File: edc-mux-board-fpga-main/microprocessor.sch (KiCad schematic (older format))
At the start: 27 parts, among them J28 PRG/SWD, J29 USB PRG, Q4 CSD22206W, Q5 CSD22206W, SW3 Reset (Microprocessor), U64 TPD3S014, U65 SAMD21JXXAM, U66 MCP1812, U67 LTC4412

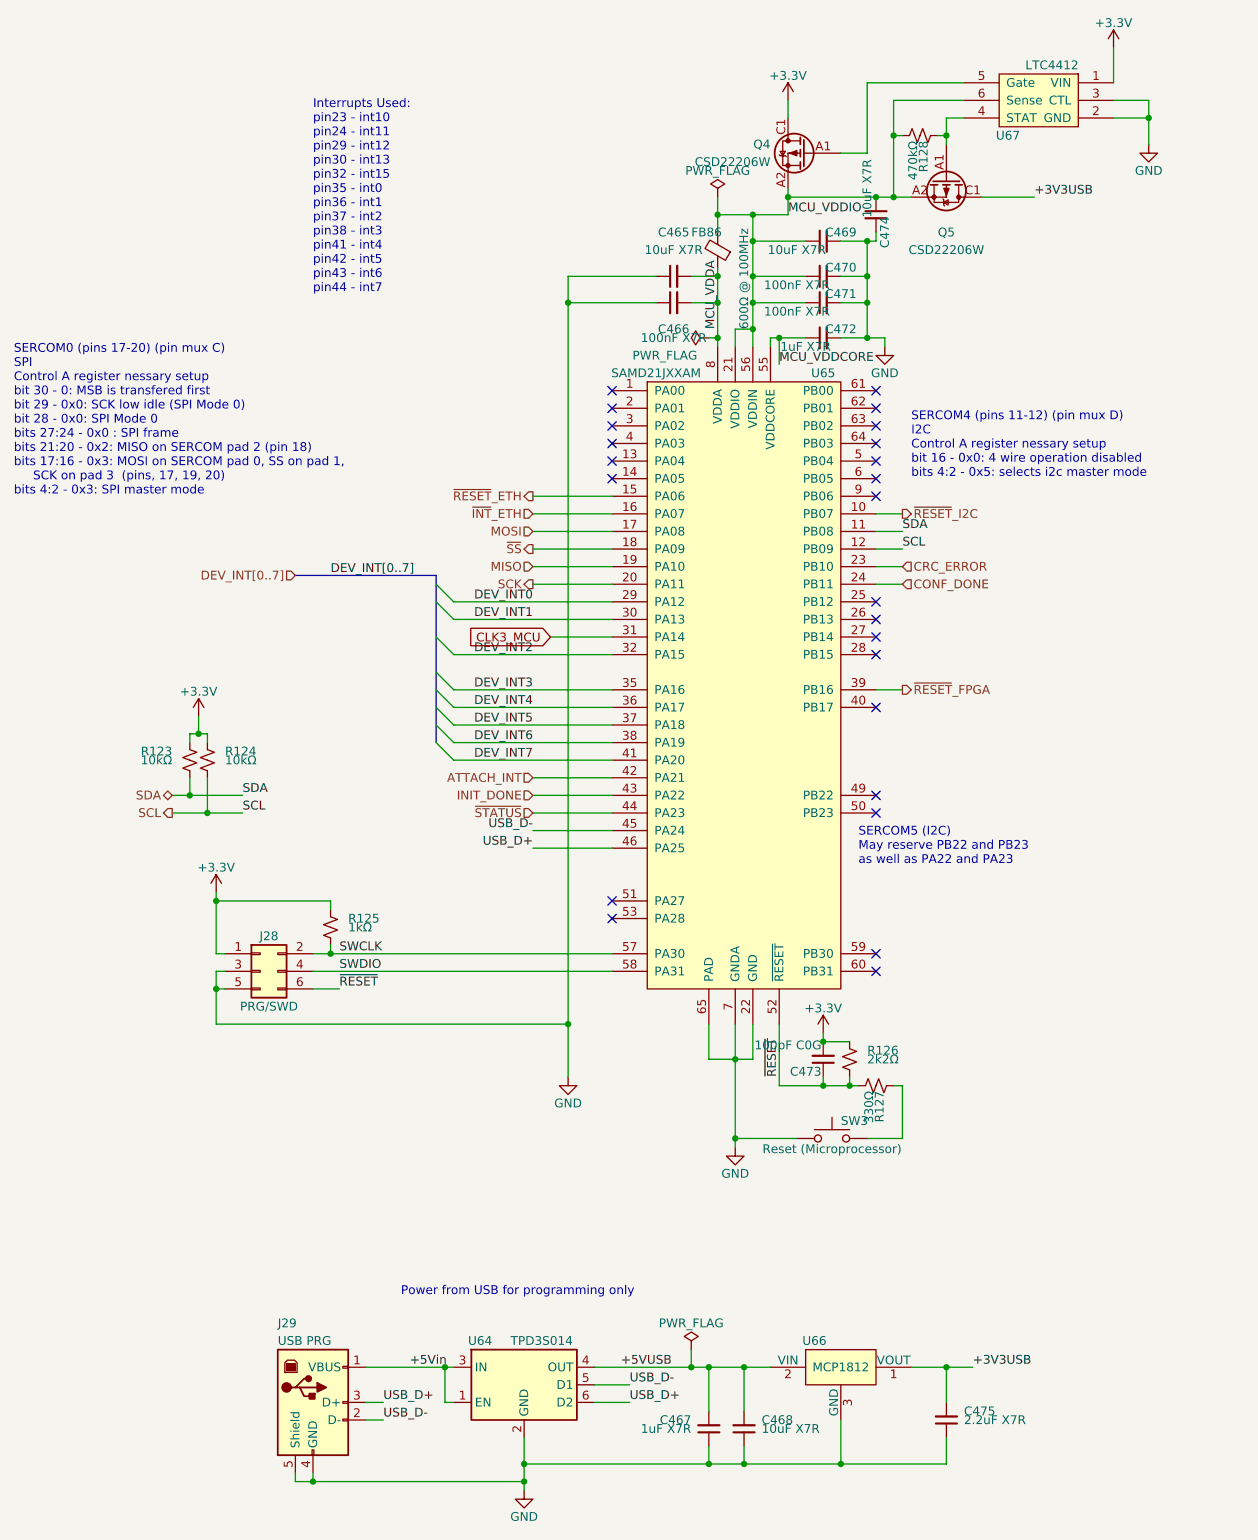
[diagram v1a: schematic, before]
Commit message: Reannotate main schematic and pcb after expansion transition
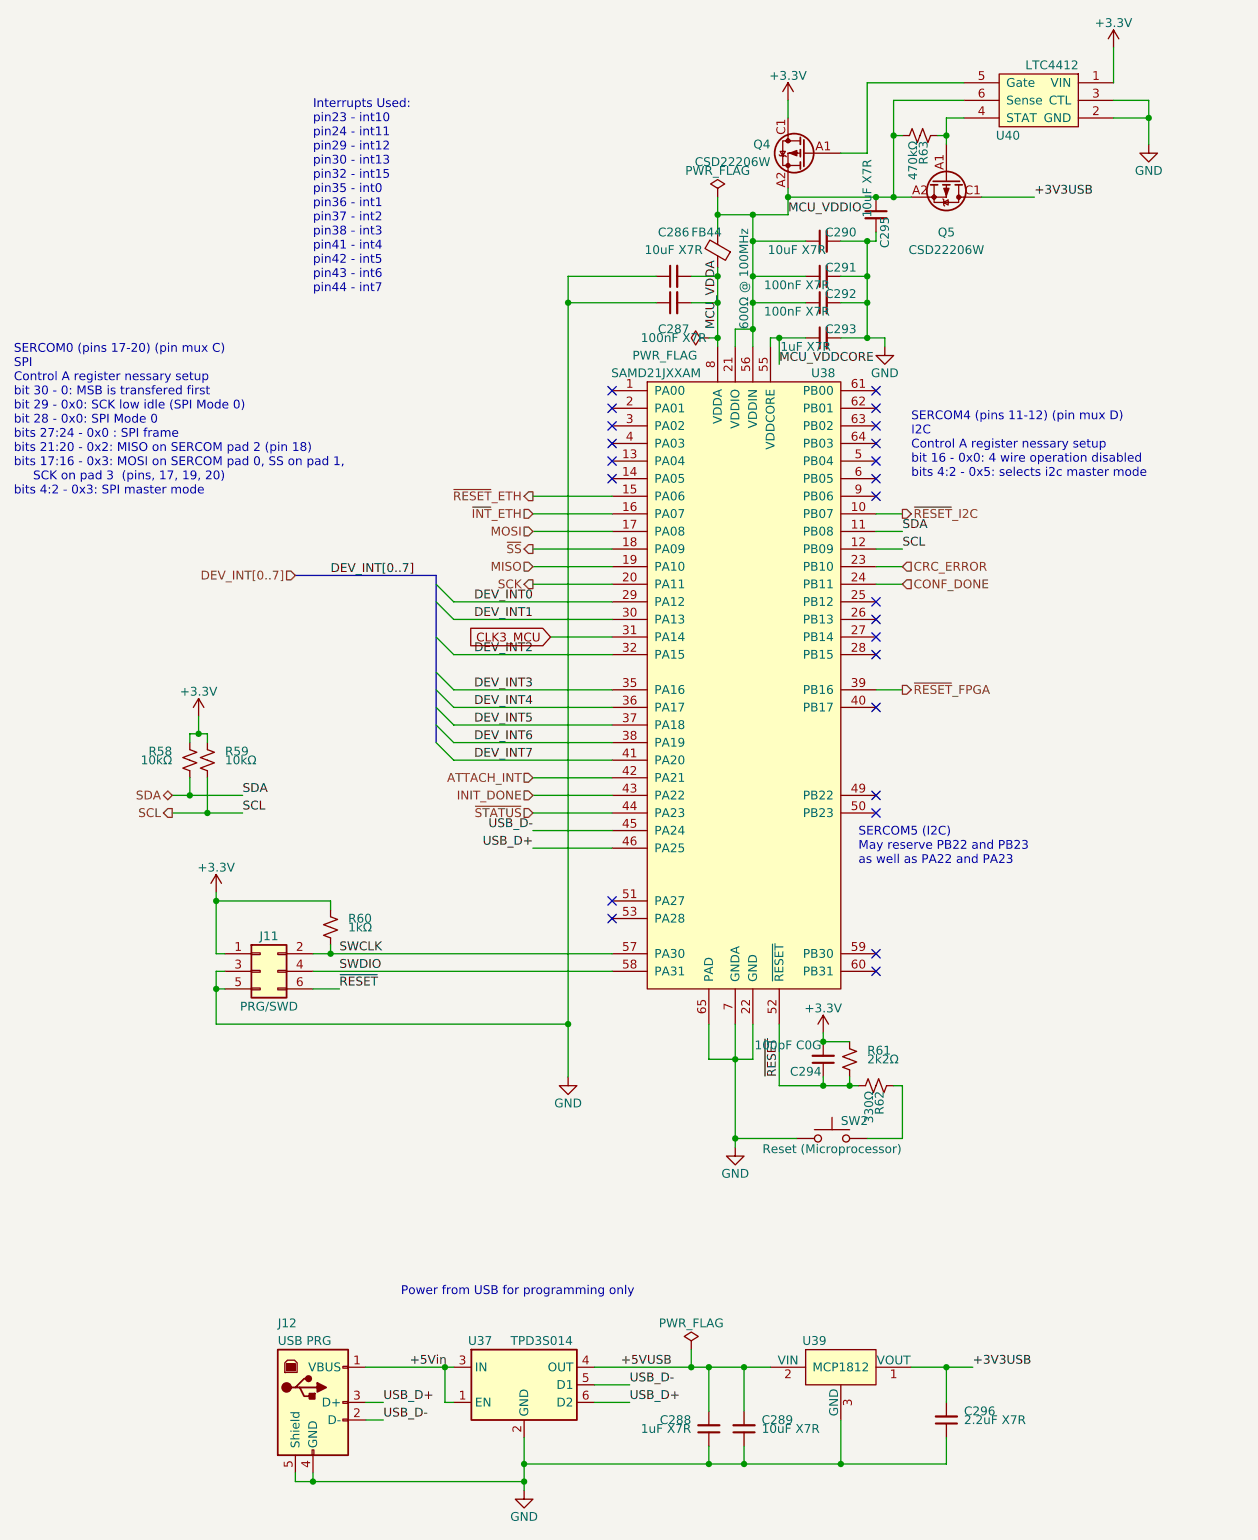
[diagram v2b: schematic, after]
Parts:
- renumbered C465 to C286, C466 to C287, C467 to C288, C468 to C289, C469 to C290, C470 to C291, C471 to C292, C472 to C293, C473 to C294, C474 to C295, C475 to C296, FB86 to FB44, J28 to J11, J29 to J12, R123 to R58, R124 to R59, R125 to R60, R126 to R61, R127 to R62, R128 to R63, SW3 to SW2, U64 to U37, U65 to U38, U66 to U39, U67 to U40

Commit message: swapping 100nF capacitors from 0603 to 0402 size
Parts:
- C287, C291, C292: footprint Capacitor_SMD:C_0603_1608Metric -> Capacitor_SMD:C_0402_1005Metric; Characteristics CAP CER 0.1UF 25V X7R 0603 -> CAP CER 0.1UF 25V X7R 0402; Manufacturer Kemet -> AVX; Manufacturers Part Number C0603C104J3RACAUTO -> 04023C104JAT2A; Package ID 0603in/1608mm -> 0402in/1005mm
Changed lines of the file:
@@
 F 0 "C287" V 3750 2300 50  0000 C CNN
 F 1 "100nF X7R" V 3700 2300 50  0000 C CNN
-F 2 "Capacitor_SMD:C_0603_1608Metric" H 3900 2300 50  0001 C CNN
-F 3 "https://content.kemet.com/datasheets/KEM_C1023_X7R_AUTO_SMD.pdf" H 3900 2300 50  0001 C CNN
-F 4 "0603in/1608mm" H 0   0   50  0001 C CNN "Package ID"
-F 5 "Kemet" H 0   0   50  0001 C CNN "Manufacturer"
-F 6 "C0603C104J3RACAUTO" H 0   0   50  0001 C CNN "Manufacturers Part Number"
-F 7 "CAP CER 0.1UF 25V X7R 0603" H 0   0   50  0001 C CNN "Characteristics"
+F 2 "Capacitor_SMD:C_0402_1005Metric" H 3900 2300 50  0001 C CNN
+F 3 "http://datasheets.avx.com/X7RDielectric.pdf" H 3900 2300 50  0001 C CNN
+F 4 "0402in/1005mm" H 0   0   50  0001 C CNN "Package ID"
+F 5 "AVX" H 0   0   50  0001 C CNN "Manufacturer"
+F 6 "04023C104JAT2A" H 0   0   50  0001 C CNN "Manufacturers Part Number"
+F 7 "CAP CER 0.1UF 25V X7R 0402" H 0   0   50  0001 C CNN "Characteristics"
 F 8 "MLCC Capacitor" H 0   0   50  0001 C CNN "Description"
 	1    3900 2300
@@
 F 0 "C291" V 4800 2050 50  0000 C CNN
 F 1 "100nF X7R" V 4700 2300 50  0000 C CNN
-F 2 "Capacitor_SMD:C_0603_1608Metric" H 4750 2150 50  0001 C CNN
-F 3 "https://content.kemet.com/datasheets/KEM_C1023_X7R_AUTO_SMD.pdf" H 4750 2150 50  0001 C CNN
-F 4 "0603in/1608mm" H 0   0   50  0001 C CNN "Package ID"
-F 5 "Kemet" H 0   0   50  0001 C CNN "Manufacturer"
-F 6 "C0603C104J3RACAUTO" H 0   0   50  0001 C CNN "Manufacturers Part Number"
-F 7 "CAP CER 0.1UF 25V X7R 0603" H 0   0   50  0001 C CNN "Characteristics"
+F 2 "Capacitor_SMD:C_0402_1005Metric" H 4750 2150 50  0001 C CNN
+F 3 "http://datasheets.avx.com/X7RDielectric.pdf" H 4750 2150 50  0001 C CNN
+F 4 "0402in/1005mm" H 0   0   50  0001 C CNN "Package ID"
+F 5 "AVX" H 0   0   50  0001 C CNN "Manufacturer"
+F 6 "04023C104JAT2A" H 0   0   50  0001 C CNN "Manufacturers Part Number"
+F 7 "CAP CER 0.1UF 25V X7R 0402" H 0   0   50  0001 C CNN "Characteristics"
 F 8 "MLCC Capacitor" H 0   0   50  0001 C CNN "Description"
 	1    4750 2150
@@
 F 0 "C292" V 4800 2200 50  0000 C CNN
 F 1 "100nF X7R" V 4700 2450 50  0000 C CNN
-F 2 "Capacitor_SMD:C_0603_1608Metric" H 4750 2300 50  0001 C CNN
-F 3 "https://content.kemet.com/datasheets/KEM_C1023_X7R_AUTO_SMD.pdf" H 4750 2300 50  0001 C CNN
-F 4 "0603in/1608mm" H 0   0   50  0001 C CNN "Package ID"
-F 5 "Kemet" H 0   0   50  0001 C CNN "Manufacturer"
-F 6 "C0603C104J3RACAUTO" H 0   0   50  0001 C CNN "Manufacturers Part Number"
-F 7 "CAP CER 0.1UF 25V X7R 0603" H 0   0   50  0001 C CNN "Characteristics"
+F 2 "Capacitor_SMD:C_0402_1005Metric" H 4750 2300 50  0001 C CNN
+F 3 "http://datasheets.avx.com/X7RDielectric.pdf" H 4750 2300 50  0001 C CNN
+F 4 "0402in/1005mm" H 0   0   50  0001 C CNN "Package ID"
+F 5 "AVX" H 0   0   50  0001 C CNN "Manufacturer"
+F 6 "04023C104JAT2A" H 0   0   50  0001 C CNN "Manufacturers Part Number"
+F 7 "CAP CER 0.1UF 25V X7R 0402" H 0   0   50  0001 C CNN "Characteristics"
 F 8 "MLCC Capacitor" H 0   0   50  0001 C CNN "Description"
 	1    4750 2300

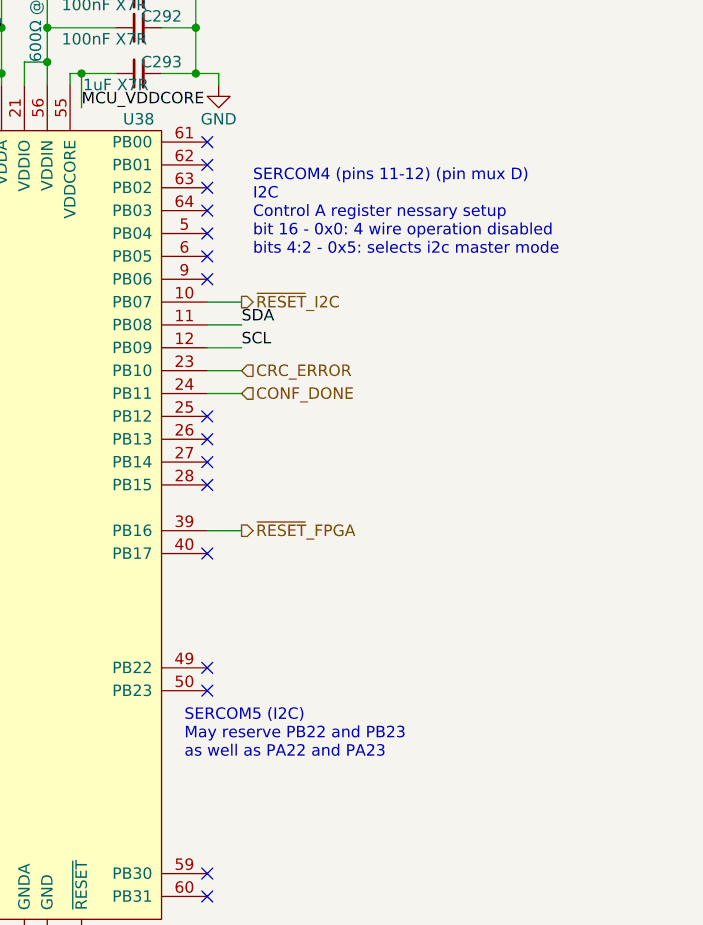
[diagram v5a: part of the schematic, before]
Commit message: swapped around a few more pins to make layout nicer
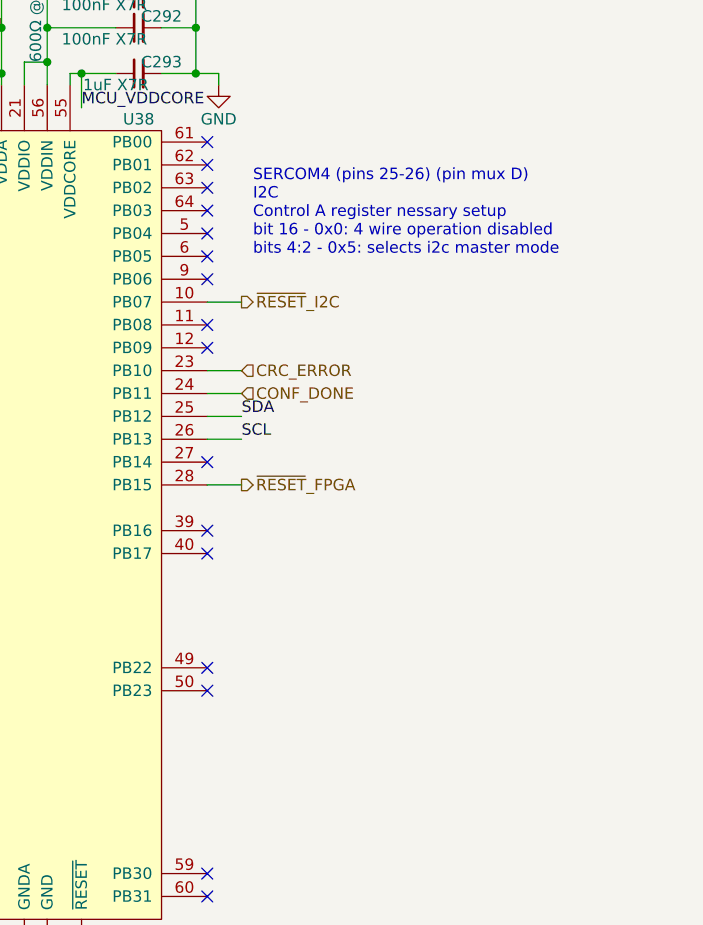
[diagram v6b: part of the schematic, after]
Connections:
- net SCL: now also U38.26 (PB13); no longer U38.12 (PB09)
- net SDA: now also U38.25 (PB12); no longer U38.11 (PB08)
- net ~RESET~_FPGA: now also U38.28 (PB15); no longer U38.39 (PB16)
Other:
- note added: "SERCOM4 (pins 25-26) (pin mux D)\nI2C\nControl A register nessary setup\nbit 16 - 0x0: 4 wire operation disabled\nbits 4:2 - 0x5: selects i2c master mode"
- note removed: "SERCOM4 (pins 11-12) (pin mux D)\nI2C\nControl A register nessary setup\nbit 16 - 0x0: 4 wire operation disabled\nbits 4:2 - 0x5: selects i2c master mode"
- note removed: "SERCOM5 (I2C)\nMay reserve PB22 and PB23\nas well as PA22 and PA23"
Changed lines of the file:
@@
 NoConn ~ 5050 5100
 NoConn ~ 5050 5200
-Text Notes 4950 5500 0    50   ~ 0
-SERCOM5 (I2C)\nMay reserve PB22 and PB23\nas well as PA22 and PA23
 Text HLabel 1750 3850 0    50   Input ~ 0
 DEV_INT[0..7]
@@
 Text HLabel 1050 5100 0    50   BiDi ~ 0
 SDA
-Text Label 5200 3600 0    50   ~ 0
+Text Label 5200 4000 0    50   ~ 0
 SDA
-Text Label 5200 3700 0    50   ~ 0
+Text Label 5200 4100 0    50   ~ 0
 SCL
 Text Label 1450 5100 0    50   ~ 0
@@
 INIT_DONE
 Wire Wire Line
-	5200 3600 5050 3600
-Wire Wire Line
-	5200 3700 5050 3700
+	5200 4000 5050 4000
+Wire Wire Line
+	5200 4100 5050 4100
 Text Label 4150 2450 1    50   ~ 0
 MCU_VDDA
@@
 Text HLabel 3100 3900 0    50   Output ~ 0
 SCK
-NoConn ~ 5050 4000
-NoConn ~ 5050 4100
 NoConn ~ 5050 4200
-NoConn ~ 5050 4300
 Text Notes 150  3400 0    50   ~ 0
 SERCOM0 (pins 17-20) (pin mux C)\nSPI\nControl A register nessary setup\nbit 30 - 0: MSB is transfered first\nbit 29 - 0x0: SCK low idle (SPI Mode 0)\nbit 28 - 0x0: SPI Mode 0\nbits 27:24 - 0x0 : SPI frame\nbits 21:20 - 0x2: MISO on SERCOM pad 2 (pin 18)\nbits 17:16 - 0x3: MOSI on SERCOM pad 0, SS on pad 1, \n     SCK on pad 3  (pins, 17, 19, 20)\nbits 4:2 - 0x3: SPI master mode\n
@@
 Text HLabel 5200 3500 2    50   Output ~ 0
 ~RESET~_I2C
-Text HLabel 5200 4500 2    50   Output ~ 0
+Text HLabel 5200 4300 2    50   Output ~ 0
 ~RESET~_FPGA
 Text Label 3100 4900 2    50   ~ 0
@@
 	5050 3500 5200 3500
 Wire Wire Line
-	5050 4500 5200 4500
+	5050 4300 5200 4300
 Text Notes 5250 3300 0    50   ~ 0
-SERCOM4 (pins 11-12) (pin mux D)\nI2C\nControl A register nessary setup\nbit 16 - 0x0: 4 wire operation disabled\nbits 4:2 - 0x5: selects i2c master mode
+SERCOM4 (pins 25-26) (pin mux D)\nI2C\nControl A register nessary setup\nbit 16 - 0x0: 4 wire operation disabled\nbits 4:2 - 0x5: selects i2c master mode
 NoConn ~ 3550 2900
 NoConn ~ 5050 3400
@@
 Wire Wire Line
 	5200 3900 5050 3900
+NoConn ~ 5050 3600
+NoConn ~ 5050 3700
+NoConn ~ 5050 4500
 Wire Bus Line
 	2550 3850 2550 4800

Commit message: Updated footprints in order to add 3d models
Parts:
- U37: footprint Package_TO_SOT_SMD:SOT-23-6 -> SW-Package-TO-SOT-SMD:SOT-23-6
- U40: footprint Package_TO_SOT_SMD:TSOT-23-6 -> SW-Package-TO-SOT-SMD:TSOT-23-6
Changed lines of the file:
@@
 F 0 "U37" H 2800 8700 50  0000 C CNN
 F 1 "TPD3S014" H 3150 8700 50  0000 C CNN
-F 2 "Package_TO_SOT_SMD:SOT-23-6" H 3050 8800 50  0001 C CNN
+F 2 "SW-Package-TO-SOT-SMD:SOT-23-6" H 3050 8800 50  0001 C CNN
 F 3 "http://www.ti.com/lit/ds/symlink/tpd3s014.pdf" H 2850 8700 50  0001 C CNN
 F 4 "ESD protection and current limiting for USB ports" H 0   0   50  0001 C CNN "Description"
@@
 F 0 "U40" H 6200 950 50  0000 C CNN
 F 1 "LTC4412" H 5950 1350 50  0000 C CNN
-F 2 "Package_TO_SOT_SMD:TSOT-23-6" H 6000 1450 50  0001 C CNN
+F 2 "SW-Package-TO-SOT-SMD:TSOT-23-6" H 6000 1450 50  0001 C CNN
 F 3 "https://www.analog.com/media/en/technical-documentation/data-sheets/4412fb.pdf" H 6550 1950 50  0001 C CNN
 F 4 "Linear Technologies" H 6000 1150 50  0001 C CNN "Manufacturer"
